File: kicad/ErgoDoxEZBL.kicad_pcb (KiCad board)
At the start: 2 copper layers, 182.8 x 158.4 mm, 95 parts, among them J1 Barrel_Jack, SW0:0 SW_Push, SW0:1 SW_Push, SW0:2 SW_Push, SW0:3 SW_Push, SW0:4 SW_Push, SW0:5 SW_Push, SW1 SW_DPST_x2, SW1:2 SW_Push, SW1:3 SW_Push, SW1:4 SW_Push, SW1:5 SW_Push, SW1:6 SW_Push, SW2:0 SW_Push, SW2:1 SW_Push, SW2:2 SW_Push, SW2:3 SW_Push, SW2:4 SW_Push, SW2:5 SW_Push, SW2:6 SW_Push, SW3:1 SW_Push, SW3:2 SW_Push, SW3:3 SW_Push, SW3:4 SW_Push, SW3:5 SW_Push, SW3:6 SW_Push, SW4:0 SW_Push, SW4:1 SW_Push, SW4:2 SW_Push, SW4:3 SW_Push, SW4:4 SW_Push, SW4:5 SW_Push, SW4:6 SW_Push, SW5:0 SW_Push, SW5:1 SW_Push, SW5:2 SW_Push, SW5:3 SW_Push, SW5:4 SW_Push, SW5:5 SW_Push

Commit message: Fix MCU position
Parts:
- moved U1 5.00 mm to (174.7, 40.5)
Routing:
- net Net-(BT1--): track 35.9 -> 29.3 mm
- net Net-(J1-PWR): track 87.1 -> 81.1 mm
- net Net-(J1-GND): track 95.6 -> 90.1 mm
- net /COL0: track 212.3 -> 207.0 mm
- net Net-(U1-RST): track 53.5 -> 48.5 mm
- net Net-(SW1A-B): track 36.8 -> 41.8 mm
- net /COL5: track 198.4 -> 193.4 mm
- net /COL4: track 221.8 -> 216.8 mm
- net /COL3: track 205.4 -> 200.4 mm
- net /COL2: track 249.1 -> 244.1 mm
- net /COL1: track 203.0 -> 198.0 mm
- net /ROW5: track 169.4 -> 165.0 mm
- net /ROW4: track 211.3 -> 214.5 mm
- net /COL6: track 90.9 -> 88.7 mm
- net /ROW2: track 234.6 -> 236.6 mm
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
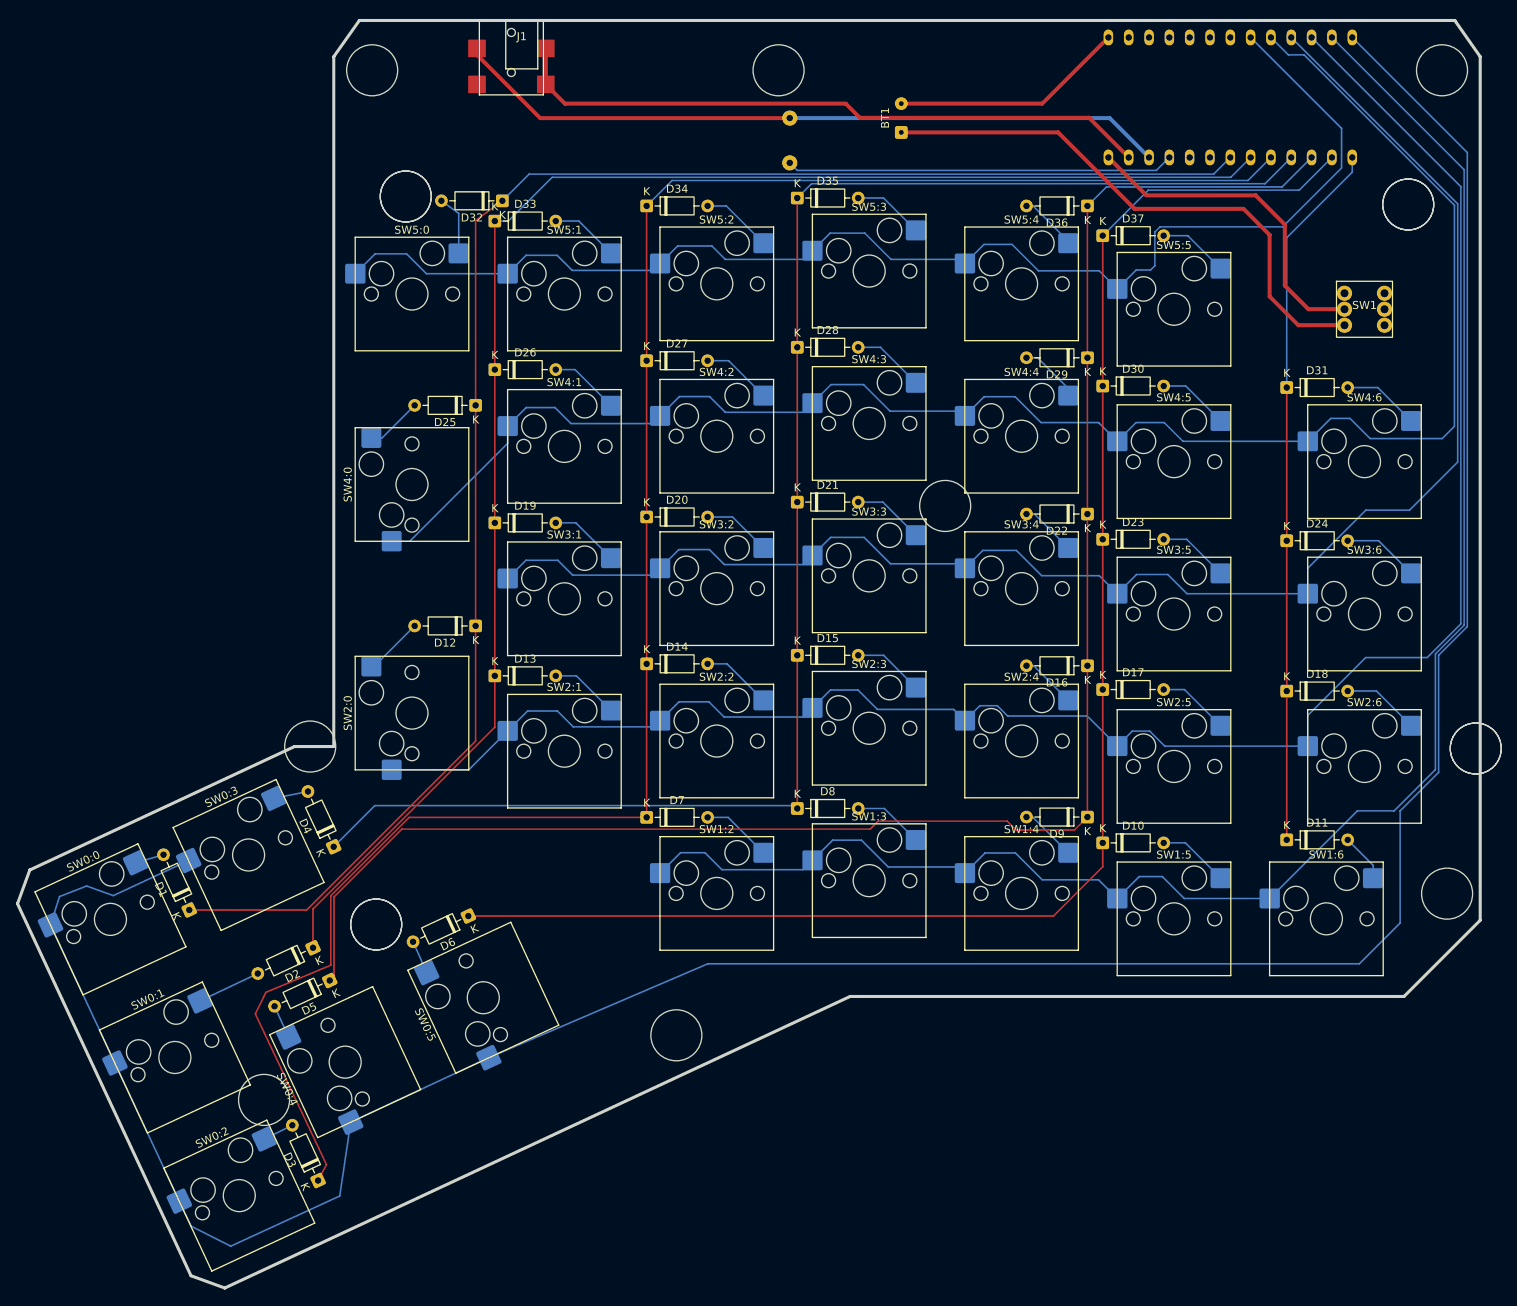
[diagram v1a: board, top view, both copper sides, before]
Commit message: PCB v2
- Fix DC jack footprint
- Single reversible PCB for both split
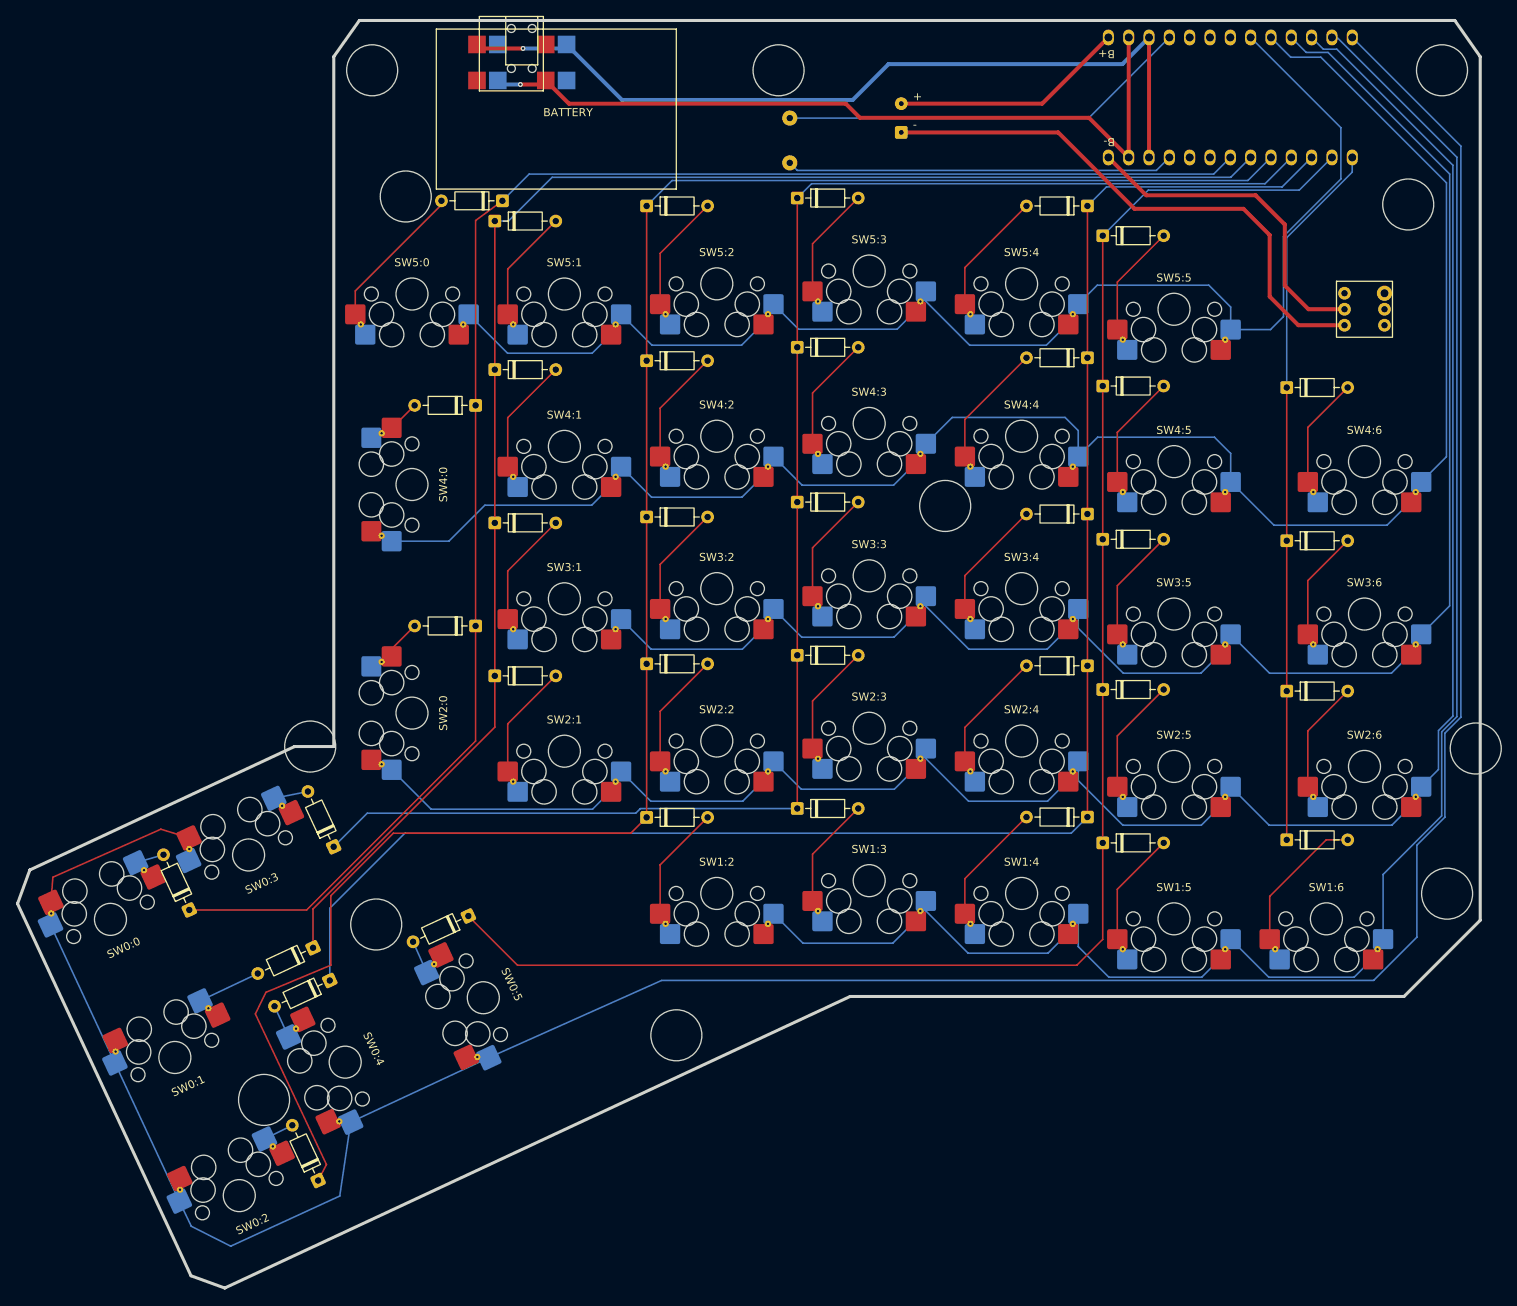
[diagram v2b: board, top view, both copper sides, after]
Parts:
- removed the ? at (196.9, 53.9)
- removed the ? at (67.9, 143.9)
- removed the ? at (71.6, 52.9)
- removed the ? at (205.4, 121.9)
- D1, D10, D11, D12, D13, D14, D15, D16, D17, D18, D19, D2, D20, D21, D22, D23, D24, D25, D26, D27, D28, D29, D3, D30, D31, D32, D33, D34, D35, D36, D37, D4, D5, D6, D7, D8, D9: footprint Diode_THT:D_DO-35_SOD27_P7.62mm_Horizontal -> Library:D_DO-35_SOD27_P7.62mm_Horizontal
- SW0:0, SW0:1, SW0:2, SW0:3, SW0:4, SW0:5, SW1:2, SW1:3, SW1:4, SW1:5, SW1:6, SW2:0, SW2:1, SW2:2, SW2:3, SW2:4, SW2:5, SW2:6, SW3:1, SW3:2, SW3:3, SW3:4, SW3:5, SW3:6, SW4:0, SW4:1, SW4:2, SW4:3, SW4:4, SW4:5, SW4:6, SW5:0, SW5:1, SW5:2, SW5:3, SW5:4, SW5:5: footprint PCM_Switch_Keyboard_Hotswap_Kailh:SW_Hotswap_Kailh_MX_1.00u -> Library:SW_Hotswap_Kailh_MX_1.00u_Reversible
- moved J1 0.50 mm to (86.1, 30.4)
- turned SW1:2 to 180 degrees
- turned SW1:3 to 180 degrees
- turned SW1:4 to 180 degrees
- turned SW1:5 to 180 degrees
- turned SW1:6 to 180 degrees
- turned SW2:1 to 180 degrees
- turned SW2:2 to 180 degrees
- turned SW2:3 to 180 degrees
- turned SW2:4 to 180 degrees
- turned SW2:5 to 180 degrees
- turned SW2:6 to 180 degrees
- turned SW3:1 to 180 degrees
- turned SW3:2 to 180 degrees
- turned SW3:3 to 180 degrees
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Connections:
- net Net-(BT1--) renamed /B-
- net Net-(SW1A-B) renamed /B+
- net Net-(U1-RST) renamed /RST
- J1 pad 1: Net-(J1-PWR) -> /RAW
- J1 pad 2: Net-(J1-GND) -> /GND2
- RST1 pad 1: Net-(J1-GND) -> /GND1
- U1 pad 2: unconnected-(U1-006-Pad2) -> /RAW
- U1 pad 24: Net-(J1-GND) -> /GND2
- U1 pad 25: Net-(J1-PWR) -> /RAW
- U1 pad 3: unconnected-(U1-008-Pad3) -> /GND2
- U1 pad 4: unconnected-(U1-GND-Pad4) -> /GND1
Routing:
- net /GND2: track 0.00 -> 104.6 mm, vias 0 -> 1
- net /RAW: track 0.00 -> 97.9 mm, vias 0 -> 1
- net Net-(J1-GND): track 90.1 -> 0.00 mm
- net Net-(J1-PWR): track 81.1 -> 0.00 mm
- net /GND1: track 0.00 -> 51.6 mm
- net /ROW2: track 236.6 -> 254.4 mm
- net Net-(D11-A): track 6.11 -> 18.0 mm
- net Net-(D32-A): track 7.67 -> 18.2 mm
- net /COL5: track 193.4 -> 203.8 mm
- net Net-(D9-A): track 7.08 -> 15.3 mm
- net Net-(D36-A): track 7.31 -> 15.5 mm
- net Net-(D16-A): track 7.02 -> 15.1 mm
- net Net-(D22-A): track 6.99 -> 15.1 mm
- net Net-(D29-A): track 7.71 -> 15.5 mm
- net Net-(D19-A): track 8.48 -> 14.5 mm
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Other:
- board text added: "B+"
- board text added: "B-"

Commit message: USB connection via TRRS jack connector
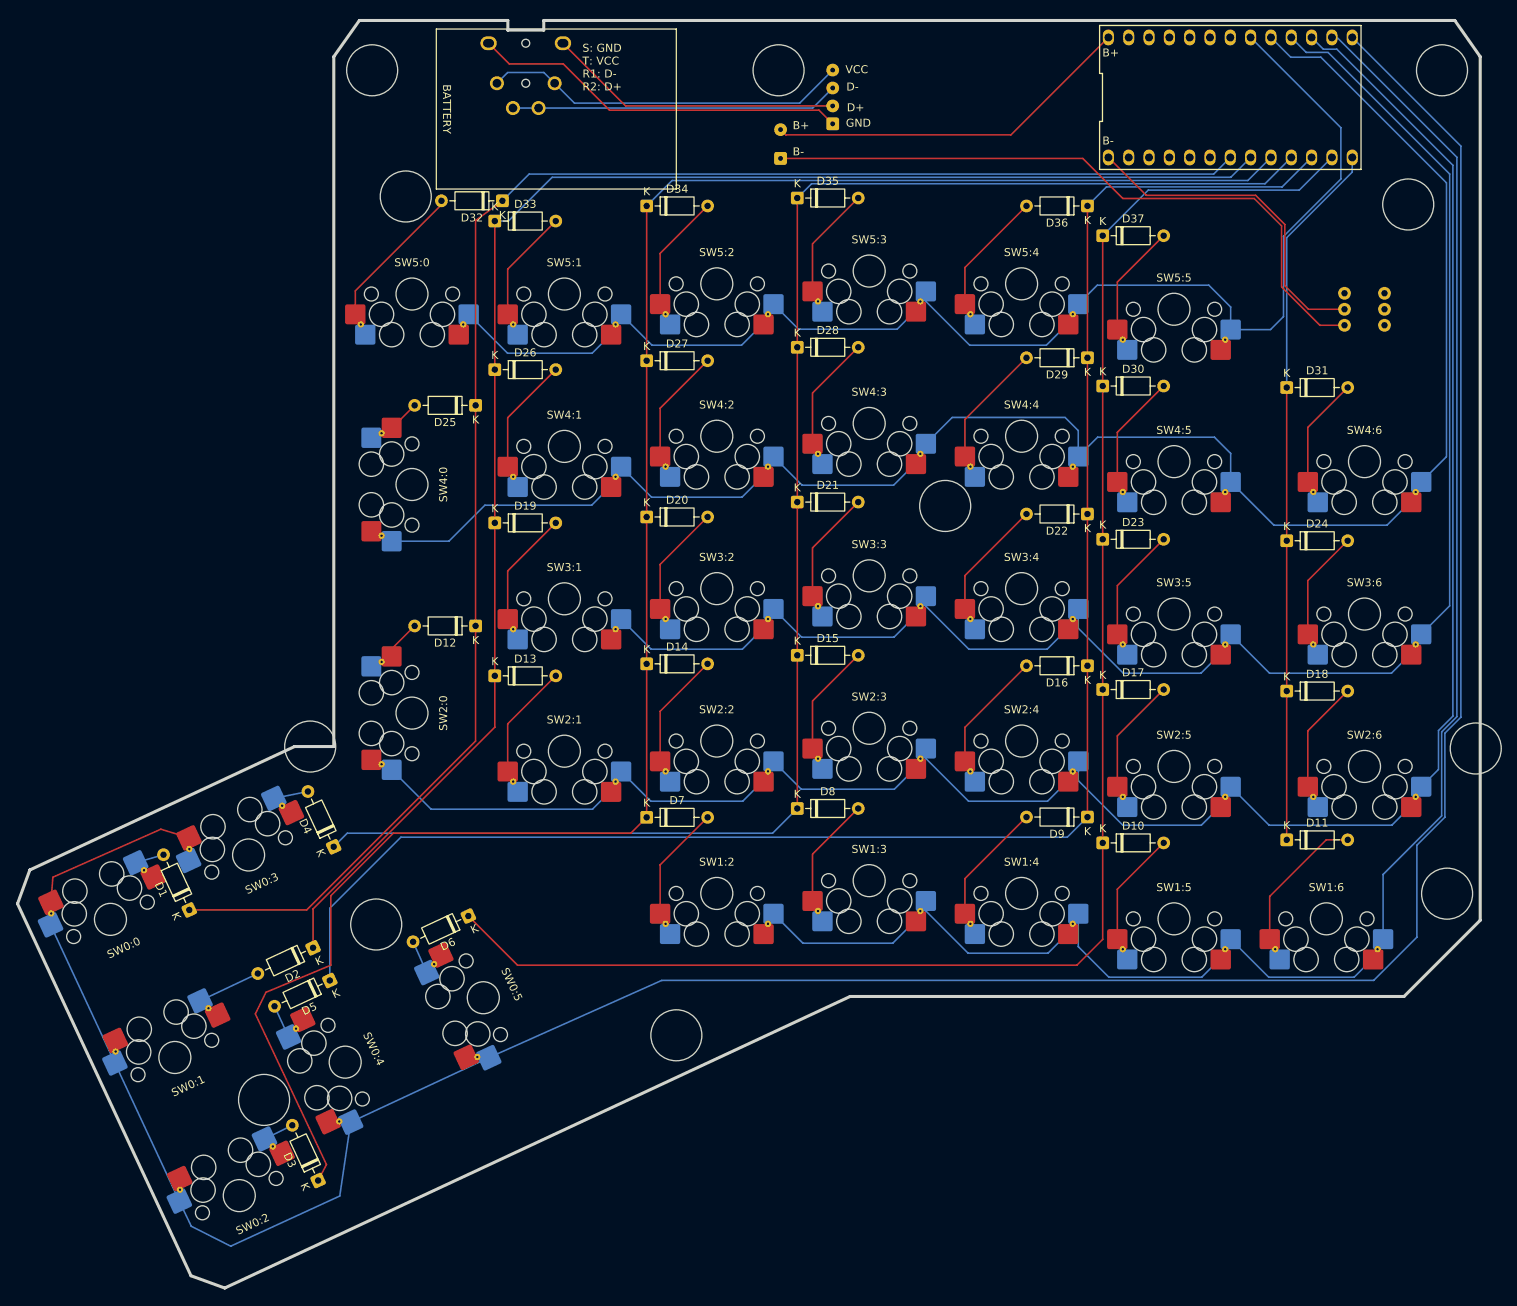
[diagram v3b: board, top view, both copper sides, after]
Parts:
- removed RST1: SW_Push, Library:Push button
- added J2: 3.5mm TRRS, Library:SJ3-35094A, F.Cu at (86.6, 33.8)
- D1, D10, D11, D12, D13, D14, D15, D16, D17, D18, D19, D2, D20, D21, D22, D23, D24, D25, D26, D27, D28, D29, D3, D30, D31, D32, D33, D34, D35, D36, D37, D4, D5, D6, D7, D8, D9: footprint Library:D_DO-35_SOD27_P7.62mm_Horizontal -> Diode_THT:D_DO-35_SOD27_P7.62mm_Horizontal
- J1: value Barrel_Jack -> USB_A; footprint Library:DC-033 -> Connector_Wire:SolderWire-0.1sqmm_1x04_P3.6mm_D0.4mm_OD1mm
- moved J1 41.1 mm to (125.0, 43.8), turned to 90 degrees
- moved BT1 15.4 mm to (118.5, 48.1)
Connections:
- J1 pad 1: /RAW -> Net-(J1-VBUS)
- J1 pad 2: /GND2 -> Net-(J1-D-)
- U1 pad 2: /RAW -> unconnected-(U1-006-Pad2)
- U1 pad 23: /RST -> unconnected-(U1-RST-Pad23)
- U1 pad 24: /GND2 -> unconnected-(U1-GND-Pad24)
- U1 pad 25: /RAW -> unconnected-(U1-RAW-Pad25)
- U1 pad 3: /GND2 -> unconnected-(U1-008-Pad3)
- U1 pad 4: /GND1 -> unconnected-(U1-GND-Pad4)
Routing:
- net /GND2: track 104.6 -> 0.00 mm, vias 1 -> 0
- net /RAW: track 97.9 -> 0.00 mm, vias 1 -> 0
- net /GND1: track 51.6 -> 0.00 mm
- net /RST: track 48.5 -> 0.00 mm
- net Net-(J1-D+): track 0.00 -> 47.2 mm
- net Net-(J1-VBUS): track 0.00 -> 45.8 mm
- net Net-(J1-D-): track 0.00 -> 41.0 mm
- net Net-(J1-GND): track 0.00 -> 37.0 mm
- net /B-: track 29.3 -> 46.3 mm
- net Net-(BT1-+): track 69.9 -> 83.6 mm
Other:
- outline, holes or cut-outs redrawn
- board text added: "D+"
- board text added: "D-"
- board text added: "GND"
- board text added: "S: GND T: VCC R1: D- R2: D+"
- board text added: "VCC"
- board text removed: "+"
- board text removed: "-"
